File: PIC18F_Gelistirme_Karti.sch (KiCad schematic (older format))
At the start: 0 parts

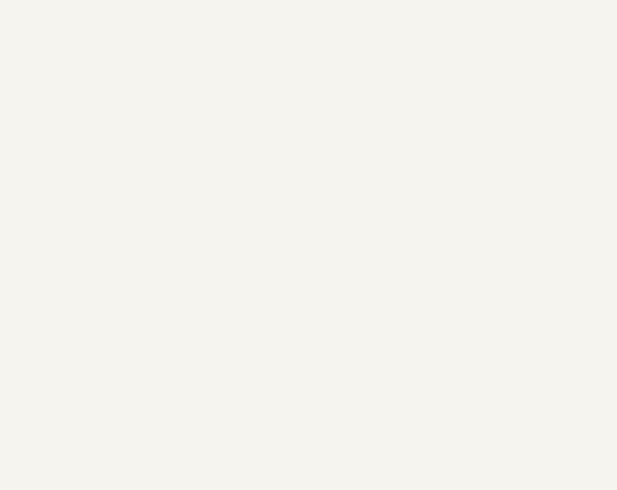
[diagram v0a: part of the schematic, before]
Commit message: LCD Blok Tasarımı
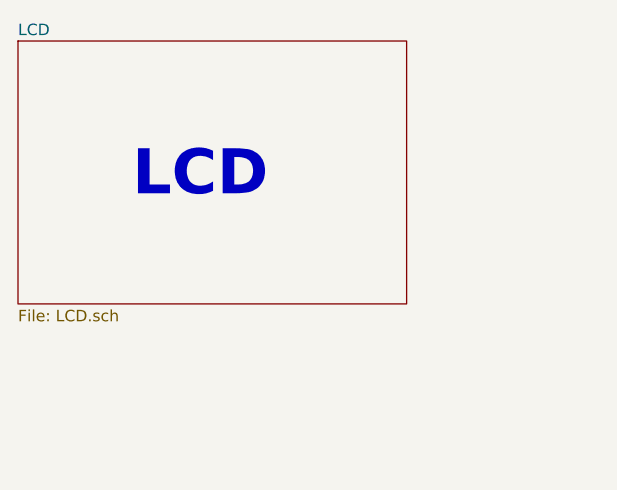
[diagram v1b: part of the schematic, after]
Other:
- note added: "LCD"
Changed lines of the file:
@@
 $Descr A4 11693 8268
 encoding utf-8
-Sheet 1 2
+Sheet 1 3
 Title "PIC18F Gelistirme Karti"
 Date ""
@@
 Text Notes 5400 3900 0    197  ~ 39
 MCU
+$Sheet
+S 1150 1200 1700 1150
+U 618AACE5
+F0 "LCD" 50
+F1 "LCD.sch" 50
+$EndSheet
+Text Notes 1650 1900 0    197  ~ 39
+LCD
 $EndSCHEMATC

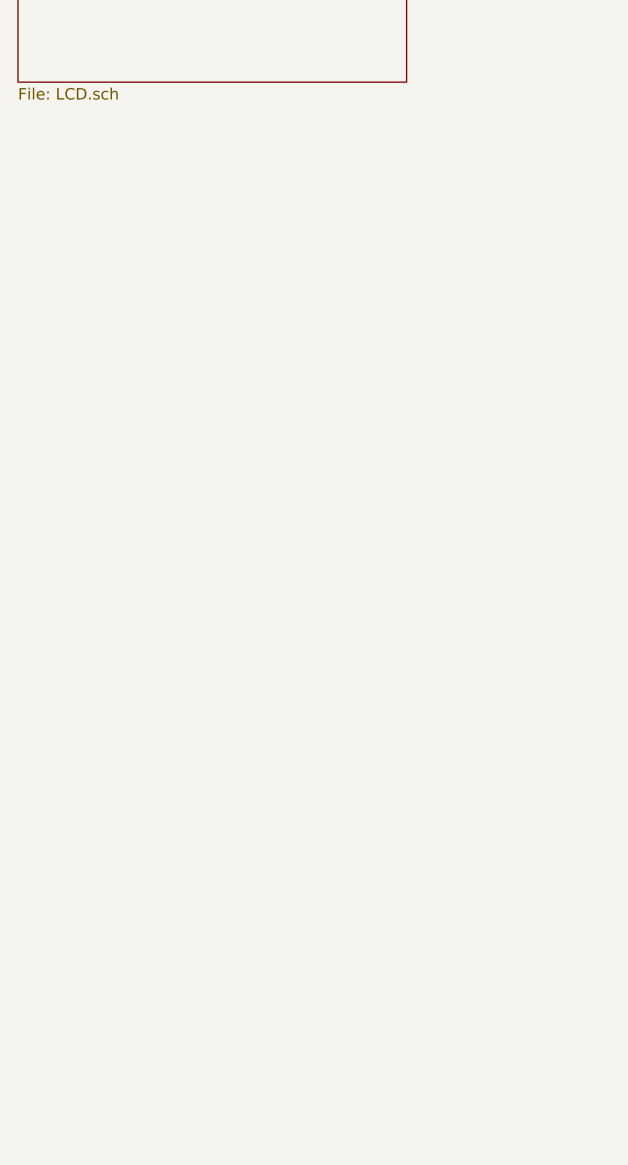
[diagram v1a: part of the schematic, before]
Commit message: LED, ADC, DISPLAY Eklendi
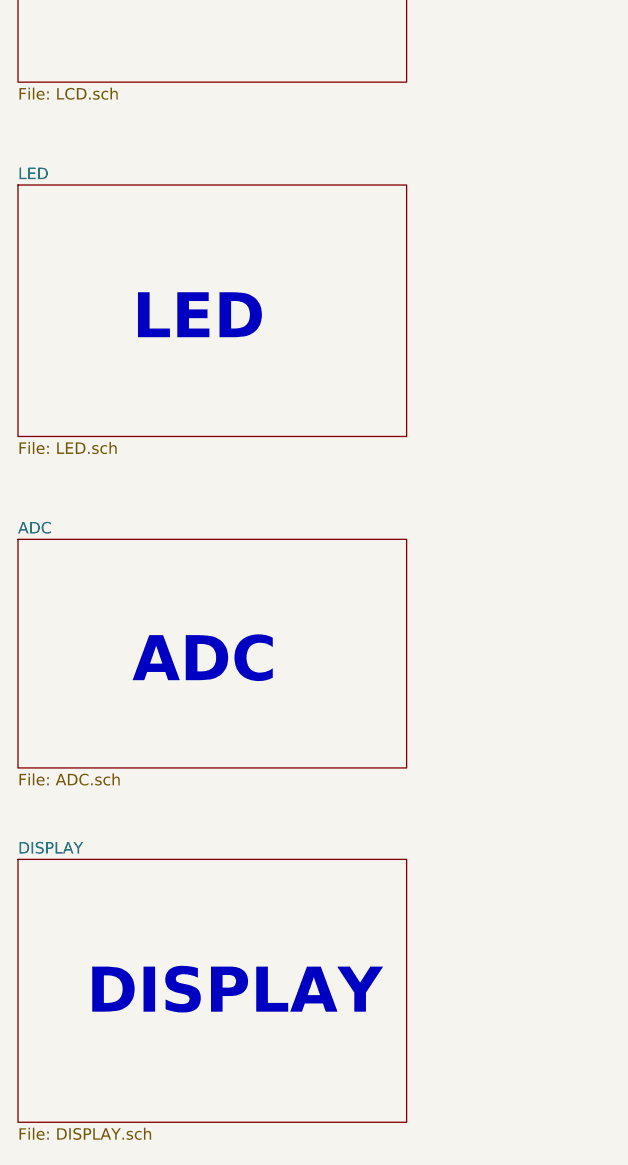
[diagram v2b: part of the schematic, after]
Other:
- note added: "ADC"
- note added: "DISPLAY"
- note added: "LED"
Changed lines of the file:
@@
 $Descr A4 11693 8268
 encoding utf-8
-Sheet 1 3
+Sheet 1 6
 Title "PIC18F Gelistirme Karti"
 Date ""
@@
 Text Notes 1650 1900 0    197  ~ 39
 LCD
+$Sheet
+S 1150 2800 1700 1100
+U 6199A67E
+F0 "LED" 50
+F1 "LED.sch" 50
+$EndSheet
+Text Notes 1650 3500 0    197  ~ 39
+LED
+$Sheet
+S 1150 4350 1700 1000
+U 619A9512
+F0 "ADC" 50
+F1 "ADC.sch" 50
+$EndSheet
+Text Notes 1650 5000 0    197  ~ 39
+ADC
+$Sheet
+S 1150 5750 1700 1150
+U 619D9715
+F0 "DISPLAY" 50
+F1 "DISPLAY.sch" 50
+$EndSheet
+Text Notes 1450 6450 0    197  ~ 39
+DISPLAY
 $EndSCHEMATC

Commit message: 6.bölüm
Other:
- note added: "BUTON\nKEYPAD\nENCODER"
- note added: "COMM"
- note added: "POWER"
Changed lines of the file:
@@
 $Descr A4 11693 8268
 encoding utf-8
-Sheet 1 6
+Sheet 1 9
 Title "PIC18F Gelistirme Karti"
 Date ""
@@
 $EndDescr
 $Sheet
-S 4900 3050 1750 1450
+S 3950 1100 1700 2700
 U 61843DE5
 F0 "MCU" 50
 F1 "MCU.sch" 50
 $EndSheet
-Text Notes 5400 3900 0    197  ~ 39
+Text Notes 4150 2700 0    394  ~ 79
 MCU
 $Sheet
-S 1150 1200 1700 1150
+S 1150 1100 1700 1150
 U 618AACE5
 F0 "LCD" 50
 F1 "LCD.sch" 50
 $EndSheet
-Text Notes 1650 1900 0    197  ~ 39
+Text Notes 1700 1800 0    197  ~ 39
 LCD
 $Sheet
-S 1150 2800 1700 1100
+S 1150 4250 1700 1150
 U 6199A67E
 F0 "LED" 50
 F1 "LED.sch" 50
 $EndSheet
-Text Notes 1650 3500 0    197  ~ 39
+Text Notes 1700 4950 0    197  ~ 39
 LED
 $Sheet
-S 1150 4350 1700 1000
+S 3950 5900 1700 1150
 U 619A9512
 F0 "ADC" 50
 F1 "ADC.sch" 50
 $EndSheet
-Text Notes 1650 5000 0    197  ~ 39
+Text Notes 4500 6650 0    197  ~ 39
 ADC
 $Sheet
-S 1150 5750 1700 1150
+S 1150 2650 1700 1150
 U 619D9715
 F0 "DISPLAY" 50
 F1 "DISPLAY.sch" 50
 $EndSheet
-Text Notes 1450 6450 0    197  ~ 39
+Text Notes 1400 3400 0    197  ~ 39
 DISPLAY
+$Sheet
+S 3950 4250 1700 1150
+U 61AE45BE
+F0 "COMMUNICATION" 50
+F1 "COMMUNICATION.sch" 50
+$EndSheet
+Text Notes 4350 4950 0    197  ~ 39
+COMM
+$Sheet
+S 1150 5900 1700 1150
+U 61C96DC0
+F0 "BUTON_KEYPAD_ENC" 50
+F1 "BUTON_KEYPAD_ENC.sch" 50
+$EndSheet
+Text Notes 1350 6950 0    197  ~ 39
+BUTON\nKEYPAD\nENCODER
+$Sheet
+S 6450 1100 1700 1150
+U 61D06C0B
+F0 "POWER" 50
+F1 "POWER.sch" 50
+$EndSheet
+Text Notes 6800 1800 0    197  ~ 39
+POWER
 $EndSCHEMATC
